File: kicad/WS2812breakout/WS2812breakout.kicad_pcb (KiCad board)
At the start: 2 copper layers, 5.4 x 9.9 mm, 3 parts, among them J3 Conn_01x04_Socket

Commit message: updated breakout schematic to include in/out lines
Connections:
- net /I2C1_SDA renamed /IN
- D3 pad 1: unconnected-(D3-DOUT-Pad1) -> /OUT
- J3 pad 3: /I2C1_SCL -> /OUT
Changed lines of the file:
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@@
 	(net 1 "+5V")
 	(net 2 "GND")
-	(net 3 "unconnected-(D3-DOUT-Pad1)")
-	(net 4 "/I2C1_SDA")
-	(net 5 "/I2C1_SCL")
+	(net 3 "/IN")
+	(net 4 "/OUT")
 	(footprint "Connector_PinHeader_2.54mm:PinHeader_1x04_P2.54mm_Vertical"
 		(layer "F.Cu")
@@
 			(layers "*.Cu" "*.Mask")
 			(remove_unused_layers no)
-			(net 4 "/I2C1_SDA")
+			(net 3 "/IN")
 			(pinfunction "Pin_2")
 			(pintype "passive")
@@
 			(layers "*.Cu" "*.Mask")
 			(remove_unused_layers no)
-			(net 5 "/I2C1_SCL")
+			(net 4 "/OUT")
 			(pinfunction "Pin_3")
-			(pintype "passive+no_connect")
+			(pintype "passive")
 		)
 		(pad "4" thru_hole oval
@@
 		(tags "capacitor")
 		(property "Reference" "C7"
-			(at 0 -1.43 270)
+			(at 0 -1.43 -90)
 			(layer "F.SilkS")
 			(effects
@@
 		)
 		(property "Value" "100 nF"
-			(at 0 1.43 270)
+			(at 0 1.43 -90)
 			(layer "F.Fab")
 			(effects
@@
 		)
 		(fp_text user "${REFERENCE}"
-			(at 0 0 270)
+			(at 0 0 -90)
 			(layer "F.Fab")
 			(effects
@@
 		(tags "LED RGB NeoPixel Nano PLCC-4 2020")
 		(property "Reference" "D3"
-			(at 0 -2 270)
+			(at 0 -2 -90)
 			(layer "F.SilkS")
 			(effects
@@
 		)
 		(property "Value" "WS2812B-2020"
-			(at 0 2.2 270)
+			(at 0 2.2 -90)
 			(layer "F.Fab")
 			(effects
@@
 		)
 		(fp_text user "${REFERENCE}"
-			(at 0 0 270)
+			(at 0 0 -90)
 			(layer "F.Fab")
 			(effects
@@
 			(size 0.7 0.7)
 			(layers "F.Cu" "F.Paste" "F.Mask")
-			(net 3 "unconnected-(D3-DOUT-Pad1)")
+			(net 4 "/OUT")
 			(pinfunction "DOUT")
-			(pintype "output+no_connect")
+			(pintype "output")
 		)
 		(pad "2" smd rect
@@
 			(size 0.7 0.7)
 			(layers "F.Cu" "F.Paste" "F.Mask")
-			(net 4 "/I2C1_SDA")
+			(net 3 "/IN")
 			(pinfunction "DIN")
 			(pintype "input")
@@
 		(width 0.2)
 		(layer "F.Cu")
-		(net 4)
+		(net 3)
 	)
 	(segment
@@
 		(width 0.2)
 		(layer "F.Cu")
-		(net 4)
+		(net 3)
 	)
 )

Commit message: Routed and Prettied-up breakout board
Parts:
- moved D3 7.72 mm to (116.3, 58.5)
- moved C7 6.92 mm to (116.3, 53.3)
- moved J3 4.96 mm to (119.5, 51.9)
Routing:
- net GND: track 9.18 -> 3.86 mm, vias 0 -> 1
- net +5V: track 13.4 -> 8.19 mm
- net /OUT: track 0.00 -> 4.97 mm
- net /IN: track 3.34 -> 4.30 mm
- added copper zone on B.Cu, net GND
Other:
- board size 5.4 x 9.9 mm -> 6.4 x 10.7 mm
- board text added: "AG/CJ"
- board text added: "Breakout v1"
- board text added: "WS2812b"

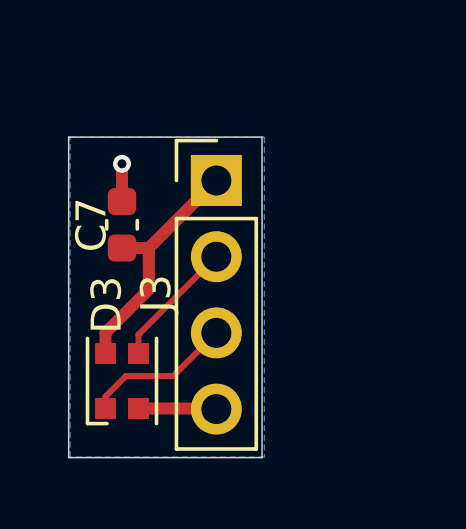
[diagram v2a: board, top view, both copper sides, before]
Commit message: Updated silkscreen for breakout
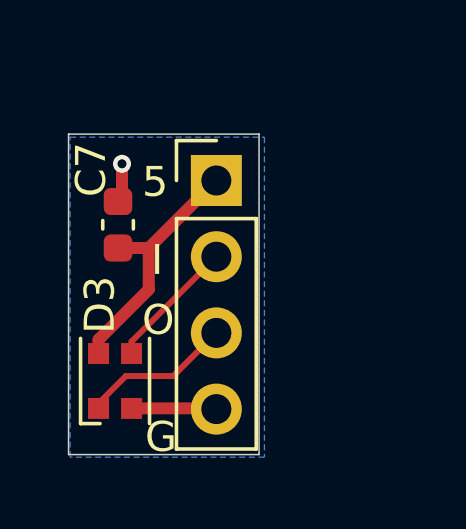
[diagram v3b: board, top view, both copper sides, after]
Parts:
- moved D3 0.23 mm to (116.1, 58.5)
- moved C7 0.13 mm to (116.2, 53.3)
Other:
- rule pad_to_mask_clearance: 0 -> 0.0508
- board text added: "5"
- board text added: "G"
- board text added: "I"
- board text added: "O"

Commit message: final fixes
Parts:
- renumbered C7 to C1, D3 to D1, J3 to J1
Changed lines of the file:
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@@
 		(descr "Through hole straight pin header, 1x04, 2.54mm pitch, single row")
 		(tags "Through hole pin header THT 1x04 2.54mm single row")
-		(property "Reference" "J3"
+		(property "Reference" "J1"
 			(at -2.002 3.762 90)
 			(layer "F.SilkS")
@@
 		(descr "Capacitor SMD 0603 (1608 Metric), square (rectangular) end terminal, IPC_7351 nominal, (Body size source: IPC-SM-782 page 76, https://www.pcb-3d.com/wordpress/wp-content/uploads/ipc-sm-782a_amendment_1_and_2.pdf), generated with kicad-footprint-generator")
 		(tags "capacitor")
-		(property "Reference" "C7"
+		(property "Reference" "C1"
 			(at 1.84 -0.9 -90)
 			(layer "F.SilkS")
@@
 		(descr "2.0mm x 2.0mm Addressable RGB LED NeoPixel Nano, 12 mA, https://cdn-shop.adafruit.com/product-files/4684/4684_WS2812B-2020_V1.3_EN.pdf")
 		(tags "LED RGB NeoPixel Nano PLCC-4 2020")
-		(property "Reference" "D3"
+		(property "Reference" "D1"
 			(at 2.54 -0.508 -90)
 			(layer "F.SilkS")
